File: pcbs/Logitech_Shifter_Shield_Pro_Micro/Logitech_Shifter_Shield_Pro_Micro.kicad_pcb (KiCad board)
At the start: 2 copper layers, 31.2 x 48.1 mm, 18 parts, among them J1 DE9_Plug_MountingHoles, J2 AVR-ISP-6, U1 SparkFun_ProMicro

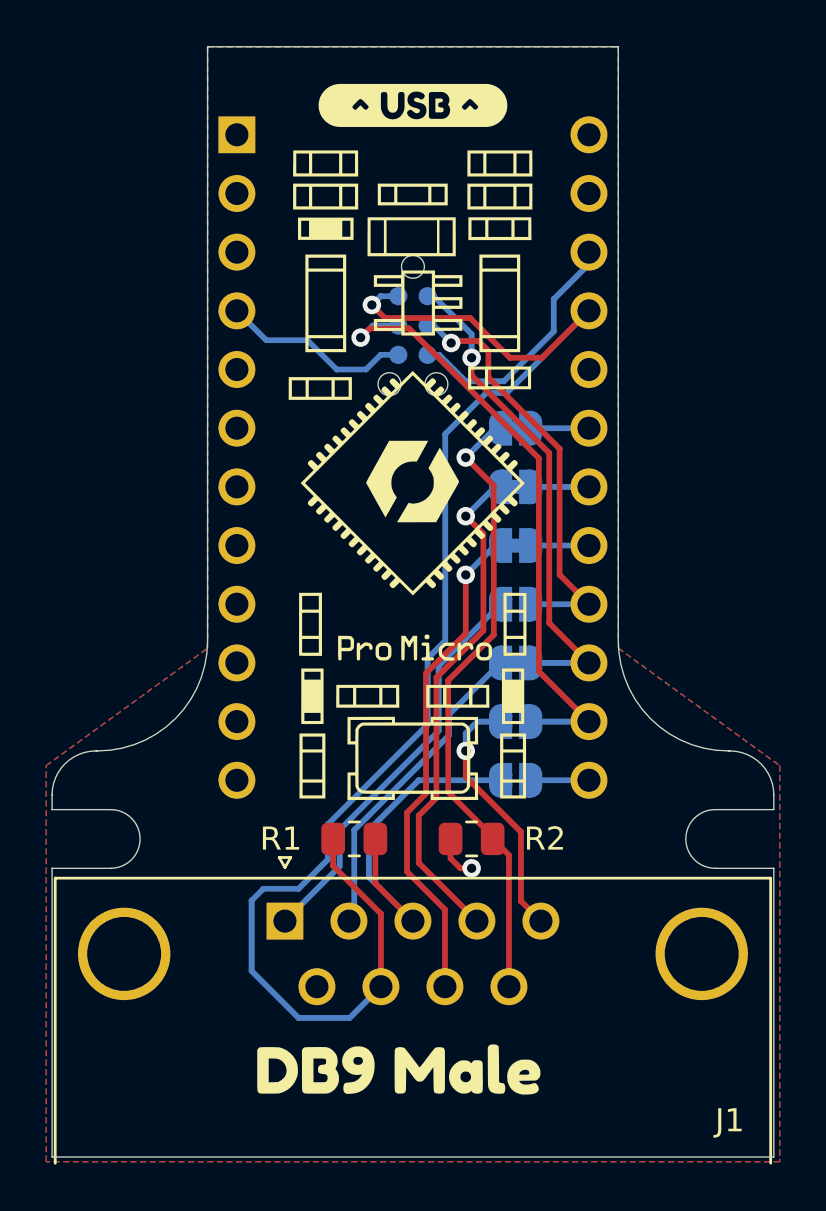
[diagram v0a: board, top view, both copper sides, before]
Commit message: Shifter: Modify PCB for G25
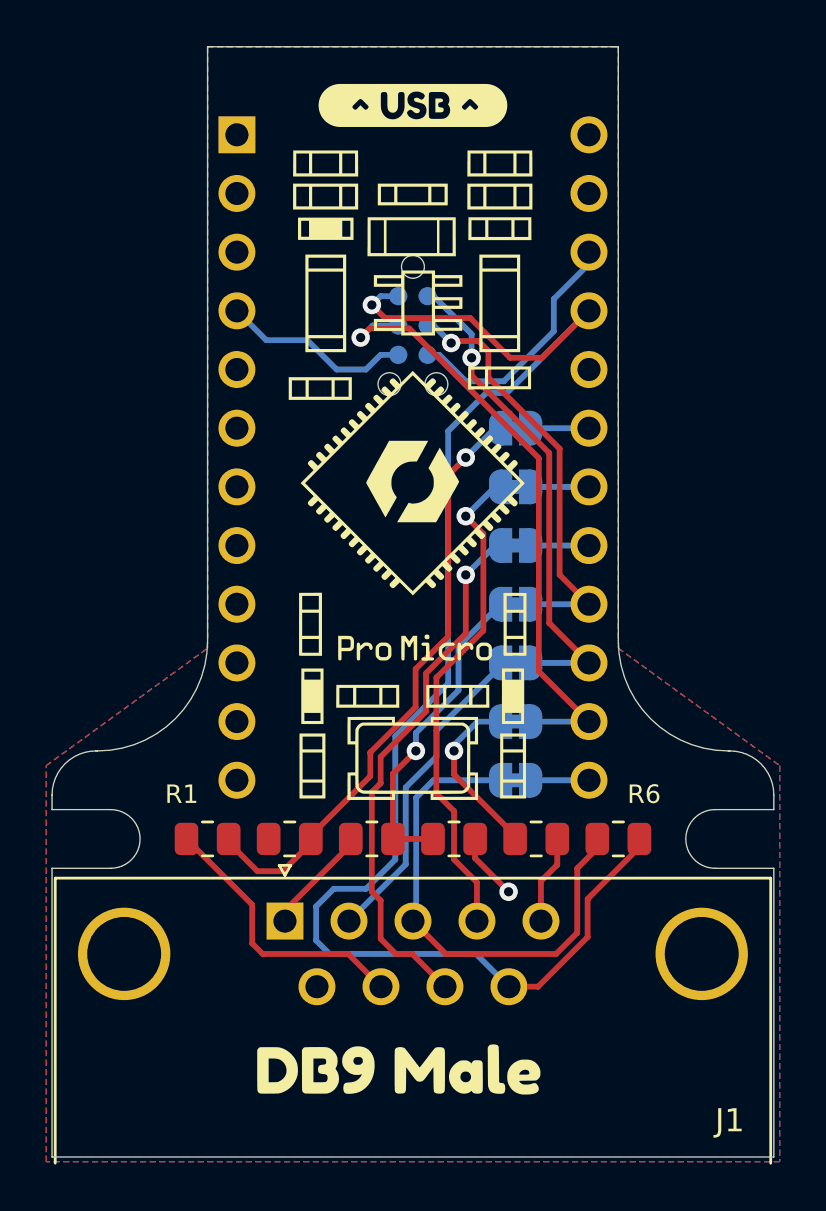
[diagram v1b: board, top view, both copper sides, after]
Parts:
- removed kibuzzard-61EDBF18: G***, kibuzzard-61EDBF18
- added G***: LOGO, Sim_Racing_Shields:Version_2.0.0, B.Cu at (152.4, 117.5)
- added R1: 470, Resistor_SMD:R_0805_2012Metric, F.Cu at (143.5, 105.4)
- added R2: 10k, Resistor_SMD:R_0805_2012Metric, F.Cu at (147.1, 105.4)
- added R5: 120, Resistor_SMD:R_0805_2012Metric, F.Cu at (157.7, 105.4)
- added R6: 10k, Resistor_SMD:R_0805_2012Metric, F.Cu at (161.3, 105.4)
- J1: footprint Connector_Dsub:DSUB-9_Male_Horizontal_P2.77x2.84mm_EdgePinOffset7.70mm_Housed_MountingHolesOffset9.12mm -> Sim_Racing_Shields:DSUB-9_Male_Horizontal_P2.77x2.84mm_EdgePinOffset7.70mm_Housed_MountingHolesOffset9.12mm_ModP1Silk
- JP1: value Detect_Jumper -> SCK_DET_Jumper
- JP2: value ShiftX_Jumper -> X_Jumper
- JP3: value ShiftY_Jumper -> Y_Jumper
- JP4: value Clock_Jumper_NC -> DET_SCK_Jumper; footprint Jumper:SolderJumper-2_P1.3mm_Open_RoundedPad1.0x1.5mm -> Sim_Racing_Shields:SolderJumper-2_P1.3mm_Bridged_RoundedPad1.0x1.5mm_Unmasked
- JP5: value Data_Jumper -> DOUT_Jumper
- JP6: value Data_In_Jumper_NC -> DIN_LED_Jumper; footprint Jumper:SolderJumper-2_P1.3mm_Open_RoundedPad1.0x1.5mm -> Sim_Racing_Shields:SolderJumper-2_P1.3mm_Bridged_RoundedPad1.0x1.5mm_Unmasked
- JP7: value CS_Jumper_NC -> CS_Jumper; footprint Jumper:SolderJumper-2_P1.3mm_Open_RoundedPad1.0x1.5mm -> Sim_Racing_Shields:SolderJumper-2_P1.3mm_Bridged_RoundedPad1.0x1.5mm_Unmasked
- R3: renamed from R1; value 10k -> 470
- moved R3 0.76 mm to (150.6, 105.4), turned to 0 degrees
- moved R4 0.76 mm to (154.2, 105.4), turned to 180 degrees
- moved G*** 0.14 mm to (152.0, 95.2)
- renumbered R2 to R4
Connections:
- net /Shift_Data renamed /Shift_DOUT
- J1 pad 1: /Shift_Clock -> Net-(J1-Pad1)
- J1 pad 5: /Shift_DataIn -> Net-(J1-Pad5)
- J1 pad 7: VCC -> Net-(J1-Pad7)
- J1 pad 9: /Shift_Detect -> VCC
- JP1 pad 2: /Shift_Detect -> /Shift_SCK_DET
- JP4 pad 2: /Shift_Clock -> /Shift_DET_SCK
- JP6 pad 2: /Shift_DataIn -> /Shift_DIN_LED
- R3 pad 1: /Shift_CS -> Net-(J1-Pad1)
- R3 pad 2: VCC -> /Shift_DET_SCK
- R4 pad 2: /Shift_Detect -> /Shift_DET_SCK
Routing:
- net /Shift_Detect: track 27.4 -> 0.00 mm, vias 1 -> 0
- net /Shift_SCK_DET: track 0.00 -> 26.2 mm, vias 0 -> 1
- net /Shift_Clock: track 17.6 -> 0.00 mm
- net /Shift_DET_SCK: track 0.00 -> 13.8 mm, vias 0 -> 1
- net Net-(J1-Pad7): track 0.00 -> 12.0 mm
- net /Shift_DataIn: track 11.2 -> 0.00 mm, vias 1 -> 0
- net /Shift_DIN_LED: track 0.00 -> 7.60 mm, vias 0 -> 1
- net /Shift_CS: track 15.6 -> 21.9 mm
- net Net-(J1-Pad1): track 0.00 -> 4.74 mm
- net Net-(J1-Pad5): track 0.00 -> 3.85 mm
- net VCC: track 62.8 -> 64.6 mm
- net /Shift_Y: track 21.6 -> 23.3 mm
- net GND: track 10.2 -> 11.2 mm
